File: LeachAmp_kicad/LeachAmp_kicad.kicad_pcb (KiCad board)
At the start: 2 copper layers, 262.4 x 104.9 mm, 124 parts, among them J1 , J2 , J3 Conn_01x03_Female, J4 Conn_01x03_Female, Q1 BC546, Q10 MPSA06, Q11 MPSA56, Q12 BF470, Q13 BF469, Q14 BF469, Q15 BF470, Q16 MJE15030, Q17 MJE15031, Q2 BC546, Q3 BC556, Q4 BC556, Q5 BC546, Q6 BC556, Q8 BC556, Q9 BC546, T1 MJL3281, T2 MJL3201, T3 MJL3281, T4 MJL3201

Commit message: oprava tranzistoru
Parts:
- J1: value (none) -> Conn_01x12_Female
- J2: value (none) -> Conn_01x04_Female
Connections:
- Q15 pad 2: Net-(C11-Pad1) -> Net-(C24-Pad1)
- Q15 pad 3: Net-(C24-Pad1) -> Net-(C11-Pad1)
- Q16 pad 1: Net-(Q16-Pad1) -> Net-(Q14-Pad1)
- Q16 pad 2: Net-(Q14-Pad1) -> Net-(C23-Pad2)
- Q16 pad 3: Net-(C23-Pad2) -> Net-(Q16-Pad3)
- Q17 pad 1: Net-(Q17-Pad1) -> Net-(Q15-Pad1)
- Q17 pad 2: Net-(Q15-Pad1) -> Net-(C24-Pad1)
- Q17 pad 3: Net-(C24-Pad1) -> Net-(Q17-Pad3)
- R36 pad 1: Net-(Q16-Pad1) -> Net-(Q16-Pad3)
- R36 pad 2: Net-(Q17-Pad1) -> Net-(Q17-Pad3)
- R41 pad 1: Net-(Q16-Pad1) -> Net-(Q16-Pad3)
- R42 pad 1: Net-(Q17-Pad1) -> Net-(Q17-Pad3)
- R43 pad 1: Net-(Q16-Pad1) -> Net-(Q16-Pad3)
- R44 pad 1: Net-(Q17-Pad1) -> Net-(Q17-Pad3)
- T1 pad 2: Net-(R37-Pad1) -> Net-(C23-Pad2)
- T1 pad 3: Net-(C23-Pad2) -> Net-(R37-Pad1)
- T2 pad 1: Net-(R38-Pad1) -> Net-(R42-Pad2)
- T2 pad 2: Net-(R42-Pad2) -> Net-(C24-Pad1)
- T2 pad 3: Net-(C24-Pad1) -> Net-(R38-Pad1)
- T3 pad 2: Net-(C19-Pad1) -> Net-(C23-Pad2)
- T3 pad 3: Net-(C23-Pad2) -> Net-(C19-Pad1)
- T4 pad 1: Net-(C20-Pad2) -> Net-(R44-Pad2)
- T4 pad 2: Net-(R44-Pad2) -> Net-(C24-Pad1)
- T4 pad 3: Net-(C24-Pad1) -> Net-(C20-Pad2)
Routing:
- net Net-(Q16-Pad1): track 82.9 -> 0.00 mm
- net Net-(Q17-Pad1): track 71.8 -> 0.00 mm
- net Net-(Q17-Pad3): track 0.00 -> 54.8 mm
- net Net-(C24-Pad1): track 217.1 -> 166.5 mm
- net Net-(C23-Pad2): track 195.9 -> 148.4 mm
- net Net-(Q16-Pad3): track 0.00 -> 45.9 mm
- net Net-(R43-Pad2): track 16.3 -> 0.00 mm
- net Net-(C19-Pad1): track 55.7 -> 42.6 mm
- net Net-(R38-Pad1): track 29.8 -> 17.1 mm
- net Net-(R37-Pad1): track 21.2 -> 9.88 mm
- net Net-(C20-Pad2): track 64.2 -> 53.5 mm
- net Net-(R44-Pad2): track 10.6 -> 0.00 mm
- net Net-(R42-Pad2): track 10.6 -> 0.00 mm
- net Net-(R41-Pad2): track 16.2 -> 6.04 mm
- net Net-(Q14-Pad1): track 26.0 -> 17.0 mm
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
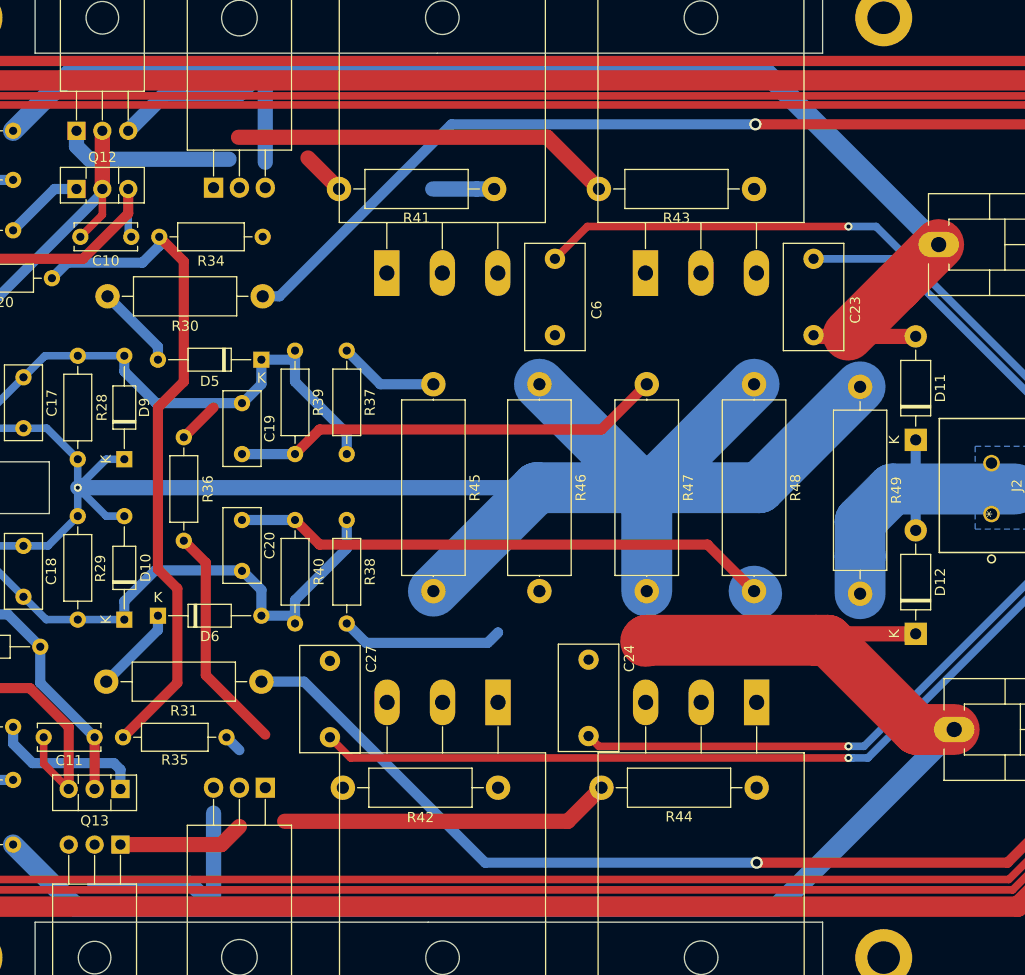
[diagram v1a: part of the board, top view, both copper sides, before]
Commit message: oprava DPS po vymene tranzistoru
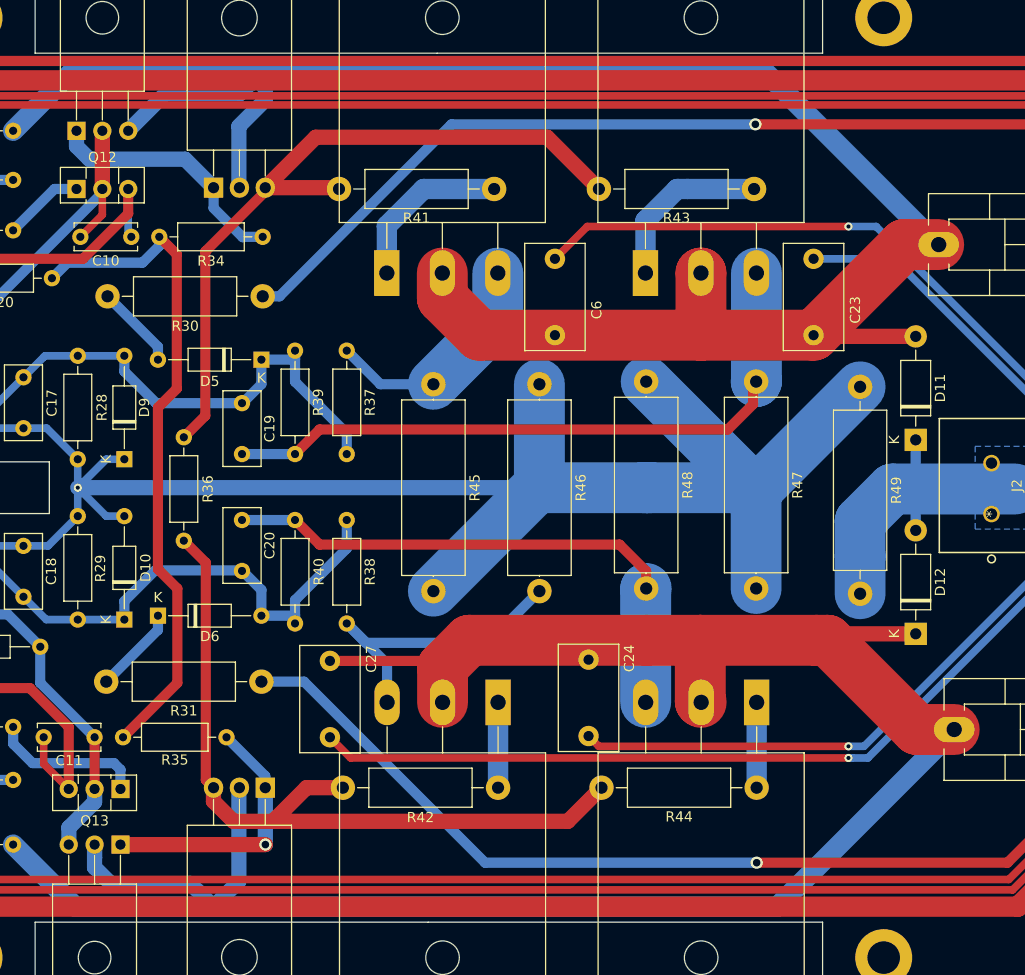
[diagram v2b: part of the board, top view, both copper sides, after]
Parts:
- moved R47 10.7 mm to (207.8, 101.3)
- moved R48 10.6 mm to (197.0, 101.3)
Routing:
- net Net-(C23-Pad2): track 148.4 -> 201.9 mm
- net Net-(C24-Pad1): track 166.5 -> 218.2 mm
- net Net-(Q16-Pad3): track 45.9 -> 72.0 mm
- net Net-(C19-Pad1): track 42.6 -> 64.9 mm
- net Net-(Q17-Pad3): track 54.8 -> 75.3 mm
- net Net-(R43-Pad2): track 0.00 -> 17.1 mm
- net Net-(R38-Pad1): track 17.1 -> 31.2 mm
- net Net-(R37-Pad1): track 9.88 -> 23.4 mm
- net Net-(Q15-Pad1): track 14.2 -> 26.4 mm, vias 0 -> 1
- net Net-(R41-Pad2): track 6.04 -> 16.7 mm
- net Net-(R44-Pad2): track 0.00 -> 8.38 mm
- net Net-(R42-Pad2): track 0.00 -> 8.38 mm
- net Net-(Q14-Pad1): track 17.0 -> 24.7 mm
- net Net-(C11-Pad1): track 44.5 -> 51.0 mm
- net Net-(C17-Pad1): track 191.9 -> 188.7 mm
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
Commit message: ladeni-DPS
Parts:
- moved R46 11.8 mm to (174.7, 101.3)
- moved R45 10.3 mm to (186.4, 101.3)
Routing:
- net Net-(R38-Pad1): track 31.2 -> 24.6 mm
- net Net-(R37-Pad1): track 23.4 -> 27.5 mm
- net Net-(C17-Pad1): track 188.7 -> 189.9 mm, vias 1 -> 0
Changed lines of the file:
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@@
     (thickness 1.6)
     (drawings 28)
-    (tracks 625)
+    (tracks 624)
     (zones 0)
     (modules 124)
@@
   )
   (setup
-    (last_trace_width 2)
+    (last_trace_width 1)
     (user_trace_width 0.75)
     (user_trace_width 1)
@@
   )
   (module Resistor_THT:R_Axial_DIN0617_L17.0mm_D6.0mm_P20.32mm_Horizontal (layer F.Cu)
-    (at 186.514 101.6 90)
+    (at 174.7 101.34 90)
     (descr "Resistor, Axial_DIN0617 series, Axial, Horizontal, pin pitch=20.32mm, 2W, length*diameter=17*6mm^2, http://www.vishay.com/docs/20128/wkxwrx.pdf")
     (tags "Resistor Axial_DIN0617 series Axial Horizontal pin pitch 20.32mm 2W length 17mm diameter 6mm")
@@
   )
   (module Resistor_THT:R_Axial_DIN0617_L17.0mm_D6.0mm_P20.32mm_Horizontal (layer F.Cu)
-    (at 176.1 101.6 90)
+    (at 186.4 101.34 90)
     (descr "Resistor, Axial_DIN0617 series, Axial, Horizontal, pin pitch=20.32mm, 2W, length*diameter=17*6mm^2, http://www.vishay.com/docs/20128/wkxwrx.pdf")
     (tags "Resistor Axial_DIN0617 series Axial Horizontal pin pitch 20.32mm 2W length 17mm diameter 6mm")
@@
   (gr_line (start 175.592 134.112) (end 136.984 134.112) (layer Edge.Cuts) (width 0.05))
   (gr_line (start 175.592 134.112) (end 214.327 134.112) (layer Edge.Cuts) (width 0.05))
-  (segment (start 82.501 93.853) (end 82.501 89.027) (width 0.75) (layer B.Cu) (net 1))
+  (segment (start 82.501 93.853) (end 82.501 89.027) (width 1) (layer B.Cu) (net 1))
   (segment (start 76.659 75.057) (end 76.659 80.01) (width 1) (layer B.Cu) (net 1))
   (segment (start 82.501 85.852) (end 82.501 89.027) (width 1) (layer B.Cu) (net 1))
@@
   (segment (start 116.607001 49.480001) (end 116.607001 49.473001) (width 1.5) (layer F.Cu) (net 4))
   (segment (start 102.567 46.863) (end 100.110999 44.406999) (width 1.5) (layer F.Cu) (net 4))
-  (segment (start 177.878 55.753) (end 207.723 55.753) (width 1) (layer B.Cu) (net 4))
-  (segment (start 159.336 72.644) (end 160.987 72.644) (width 1) (layer B.Cu) (net 4))
-  (segment (start 160.987 72.644) (end 177.878 55.753) (width 1) (layer B.Cu) (net 4))
   (segment (start 207.723 55.753) (end 207.723 55.753) (width 1) (layer B.Cu) (net 4))
   (via (at 207.723 55.753) (size 1.2) (drill 0.75) (layers F.Cu B.Cu) (net 4))
@@
   (segment (start 117.172 52.959) (end 234.901 52.959) (width 0.75) (layer F.Cu) (net 4))
   (segment (start 234.901 52.959) (end 240.235 58.293) (width 0.75) (layer F.Cu) (net 4))
-  (segment (start 234.393 53.848) (end 239.219 58.674) (width 0.75) (layer F.Cu) (net 4))
-  (segment (start 116.664 53.848) (end 234.393 53.848) (width 0.75) (layer F.Cu) (net 4))
-  (segment (start 239.219 58.674) (end 239.219 86.233) (width 0.75) (layer F.Cu) (net 4))
-  (segment (start 114.505 51.689) (end 116.664 53.848) (width 0.75) (layer F.Cu) (net 4))
-  (segment (start 100.909 58.413) (end 100.916 58.42) (width 0.75) (layer F.Cu) (net 4))
-  (segment (start 100.154 58.413) (end 100.909 58.413) (width 0.75) (layer F.Cu) (net 4))
-  (segment (start 100.916 58.42) (end 101.297 58.42) (width 0.75) (layer F.Cu) (net 4))
-  (segment (start 243.537 90.551) (end 245.95 90.551) (width 0.75) (layer F.Cu) (net 4))
-  (segment (start 239.219 86.233) (end 243.537 90.551) (width 0.75) (layer F.Cu) (net 4))
-  (segment (start 101.297 58.42) (end 108.028 51.689) (width 0.75) (layer F.Cu) (net 4))
-  (segment (start 108.028 51.689) (end 114.505 51.689) (width 0.75) (layer F.Cu) (net 4))
   (segment (start 246.458 93.98) (end 246.204 93.98) (width 2) (layer F.Cu) (net 4))
   (segment (start 243.029 123.063) (end 233.504 132.588) (width 2) (layer F.Cu) (net 4))
@@
   (segment (start 240.489 122.047) (end 240.489 96.012) (width 0.75) (layer F.Cu) (net 4))
   (segment (start 244.045 92.456) (end 246.077 92.456) (width 0.75) (layer F.Cu) (net 4))
+  (segment (start 243.537 90.551) (end 245.95 90.551) (width 0.75) (layer F.Cu) (net 4))
+  (segment (start 239.219 86.233) (end 243.537 90.551) (width 0.75) (layer F.Cu) (net 4))
+  (segment (start 239.219 58.674) (end 239.219 86.233) (width 0.75) (layer F.Cu) (net 4))
+  (segment (start 234.393 53.848) (end 239.219 58.674) (width 0.75) (layer F.Cu) (net 4))
+  (segment (start 114.505 51.689) (end 116.664 53.848) (width 0.75) (layer F.Cu) (net 4))
+  (segment (start 100.909 58.413) (end 100.916 58.42) (width 0.75) (layer F.Cu) (net 4))
+  (segment (start 100.154 58.413) (end 100.909 58.413) (width 0.75) (layer F.Cu) (net 4))
+  (segment (start 100.916 58.42) (end 102.37 58.42) (width 0.75) (layer F.Cu) (net 4))
+  (segment (start 109.101 51.689) (end 114.505 51.689) (width 0.75) (layer F.Cu) (net 4))
+  (segment (start 116.664 53.848) (end 234.393 53.848) (width 0.75) (layer F.Cu) (net 4))
+  (segment (start 102.37 58.42) (end 109.101 51.689) (width 0.75) (layer F.Cu) (net 4))
+  (segment (start 177.487 55.753) (end 207.723 55.753) (width 1) (layer B.Cu) (net 4))
+  (segment (start 159.336 72.644) (end 160.596 72.644) (width 1) (layer B.Cu) (net 4))
+  (segment (start 160.596 72.644) (end 177.487 55.753) (width 1) (layer B.Cu) (net 4))
   (segment (start 85.93 114.783998) (end 87.683998 113.03) (width 0.75) (layer B.Cu) (net 5))
   (segment (start 85.93 115.824) (end 85.93 114.783998) (width 0.75) (layer B.Cu) (net 5))
@@
   (segment (start 137.953 78.486) (end 137.826 78.613) (width 0.75) (layer B.Cu) (net 17))
   (segment (start 141.175 78.486) (end 137.953 78.486) (width 0.75) (layer B.Cu) (net 17))
-  (via (at 141.175 91.44) (size 0.8) (drill 0.4) (layers F.Cu B.Cu) (net 18))
   (segment (start 186.26 91.44) (end 197.055 91.44) (width 5) (layer B.Cu) (net 18))
-  (segment (start 176.1 101.6) (end 186.26 91.44) (width 5) (layer B.Cu) (net 18))
   (segment (start 197.055 91.44) (end 197.436 91.44) (width 5) (layer B.Cu) (net 18))
   (segment (start 208.104 91.44) (end 218.01 81.534) (width 5) (layer B.Cu) (net 18))
@@
   (segment (start 207.8 91.744) (end 207.8 101.34) (width 5) (layer B.Cu) (net 18))
   (segment (start 208.104 91.44) (end 207.8 91.744) (width 5) (layer B.Cu) (net 18))
-  (segment (start 186.514 91.186) (end 186.514 81.28) (width 5) (layer B.Cu) (net 18))
-  (segment (start 186.26 91.44) (end 186.514 91.186) (width 5) (layer B.Cu) (net 18))
   (segment (start 207.42 91.44) (end 197 81.02) (width 5) (layer B.Cu) (net 18))
   (segment (start 208.104 91.44) (end 207.42 91.44) (width 5) (layer B.Cu) (net 18))
+  (segment (start 185.12 91.44) (end 174.7 81.02) (width 5) (layer B.Cu) (net 18))
+  (segment (start 186.26 91.44) (end 185.12 91.44) (width 5) (layer B.Cu) (net 18))
+  (segment (start 186.4 91.58) (end 186.4 101.34) (width 5) (layer B.Cu) (net 18))
+  (segment (start 186.26 91.44) (end 186.4 91.58) (width 5) (layer B.Cu) (net 18))
   (segment (start 141.175 104.394) (end 145.747 104.394) (width 0.75) (layer B.Cu) (net 19))
   (segment (start 145.747 102.594) (end 145.747 104.394) (width 1) (layer B.Cu) (net 19))
@@
   (segment (start 176.179 108.451) (end 177 109.272) (width 1) (layer F.Cu) (net 24))
   (segment (start 165.94 108.451) (end 176.179 108.451) (width 1) (layer F.Cu) (net 24))
-  (segment (start 202.314 112.436) (end 202.4 112.522) (width 5) (layer F.Cu) (net 24))
   (segment (start 202.314 106.426) (end 202.314 112.436) (width 5) (layer F.Cu) (net 24))
   (segment (start 202.314 106.426) (end 213.692 106.426) (width 5) (layer F.Cu) (net 24))
@@
   (segment (start 92.698999 89.826999) (end 91.899 89.027) (width 1) (layer B.Cu) (net 50))
   (segment (start 104.472 104.521) (end 94.185 94.234) (width 1) (layer B.Cu) (net 50))
-  (segment (start 87.327 93.853) (end 91.899 93.853) (width 0.75) (layer B.Cu) (net 51))
+  (segment (start 87.327 93.853) (end 91.899 93.853) (width 1) (layer B.Cu) (net 51))
   (segment (start 101.297 82.296) (end 105.869 77.724) (width 1) (layer B.Cu) (net 51))
   (segment (start 89.613 87.757) (end 95.074 82.296) (width 1) (layer B.Cu) (net 51))
@@
   (segment (start 116.664 104.521) (end 123.649 104.521) (width 1) (layer F.Cu) (net 53))
   (segment (start 123.649 104.521) (end 124.919 103.251) (width 1) (layer F.Cu) (net 53))
-  (segment (start 170.893 81.28) (end 176.1 81.28) (width 1) (layer B.Cu) (net 54))
-  (segment (start 167.591 77.978) (end 170.893 81.28) (width 1) (layer B.Cu) (net 54))
-  (segment (start 182.428 74.952) (end 182.428 70.358) (width 5) (layer B.Cu) (net 54))
-  (segment (start 176.1 81.28) (end 182.428 74.952) (width 5) (layer B.Cu) (net 54))
+  (segment (start 182.428 77.048) (end 186.4 81.02) (width 5) (layer B.Cu) (net 54))
+  (segment (start 182.428 70.358) (end 182.428 77.048) (width 5) (layer B.Cu) (net 54))
+  (segment (start 168.521 77.048) (end 167.591 77.978) (width 1) (layer B.Cu) (net 54))
+  (segment (start 182.428 77.048) (end 168.521 77.048) (width 1) (layer B.Cu) (net 54))
   (segment (start 167.591 104.775) (end 169.496 106.68) (width 1) (layer B.Cu) (net 55))
-  (segment (start 169.496 106.68) (end 181.434 106.68) (width 1) (layer B.Cu) (net 55))
-  (segment (start 181.434 106.68) (end 186.514 101.6) (width 1) (layer B.Cu) (net 55))
   (segment (start 171.55 108.734) (end 167.591 104.775) (width 1) (layer B.Cu) (net 55))
   (segment (start 171.55 112.522) (end 171.55 108.734) (width 1) (layer B.Cu) (net 55))
+  (segment (start 171.55 104.49) (end 174.7 101.34) (width 5) (layer B.Cu) (net 55))
+  (segment (start 171.55 112.522) (end 171.55 104.49) (width 5) (layer B.Cu) (net 55))
   (segment (start 182.069 62.103) (end 175.137 62.103) (width 2) (layer B.Cu) (net 56))
   (segment (start 171.528 65.712) (end 171.528 70.358) (width 2) (layer B.Cu) (net 56))

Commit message: 100% DPS
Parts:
- J1: value Conn_01x12_Female -> (none)
- J2: value Conn_01x04_Female -> (none)
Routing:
- net GND: track 2025.4 -> 2030.0 mm
- net Net-(R38-Pad1): track 24.6 -> 20.6 mm
- net Net-(C24-Pad1): track 218.1 -> 215.4 mm
- net Net-(C20-Pad2): track 54.7 -> 53.7 mm
- net Net-(R37-Pad1): track 27.5 -> 28.4 mm
- net Net-(C19-Pad1): track 64.9 -> 64.1 mm
- net Net-(C9-Pad1): track 32.6 -> 32.0 mm
- net Net-(C18-Pad1): track 55.3 -> 54.7 mm
- net Net-(C17-Pad2): track 54.1 -> 53.6 mm
- net GNDS: vias 2 -> 0
